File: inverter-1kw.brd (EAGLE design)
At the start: 96.6 x 100 mm, 189 parts, among them IC1 LMV358MMX, IC2 LMV358MMX, Q4 1200980569**TRANS SMD NPN MMB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, Q6 1200980569**TRANS SMD NPN MMB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, U1 ACS712, U4 ACS712, U5 SI8230, U6 SI8230, U7 ACS712, X2 https://ozdisan.com/connector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, X3 https://ozdisan.com/connector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, X7 https://ozdisan.com/connector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, X8 https://ozdisan.com/connector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

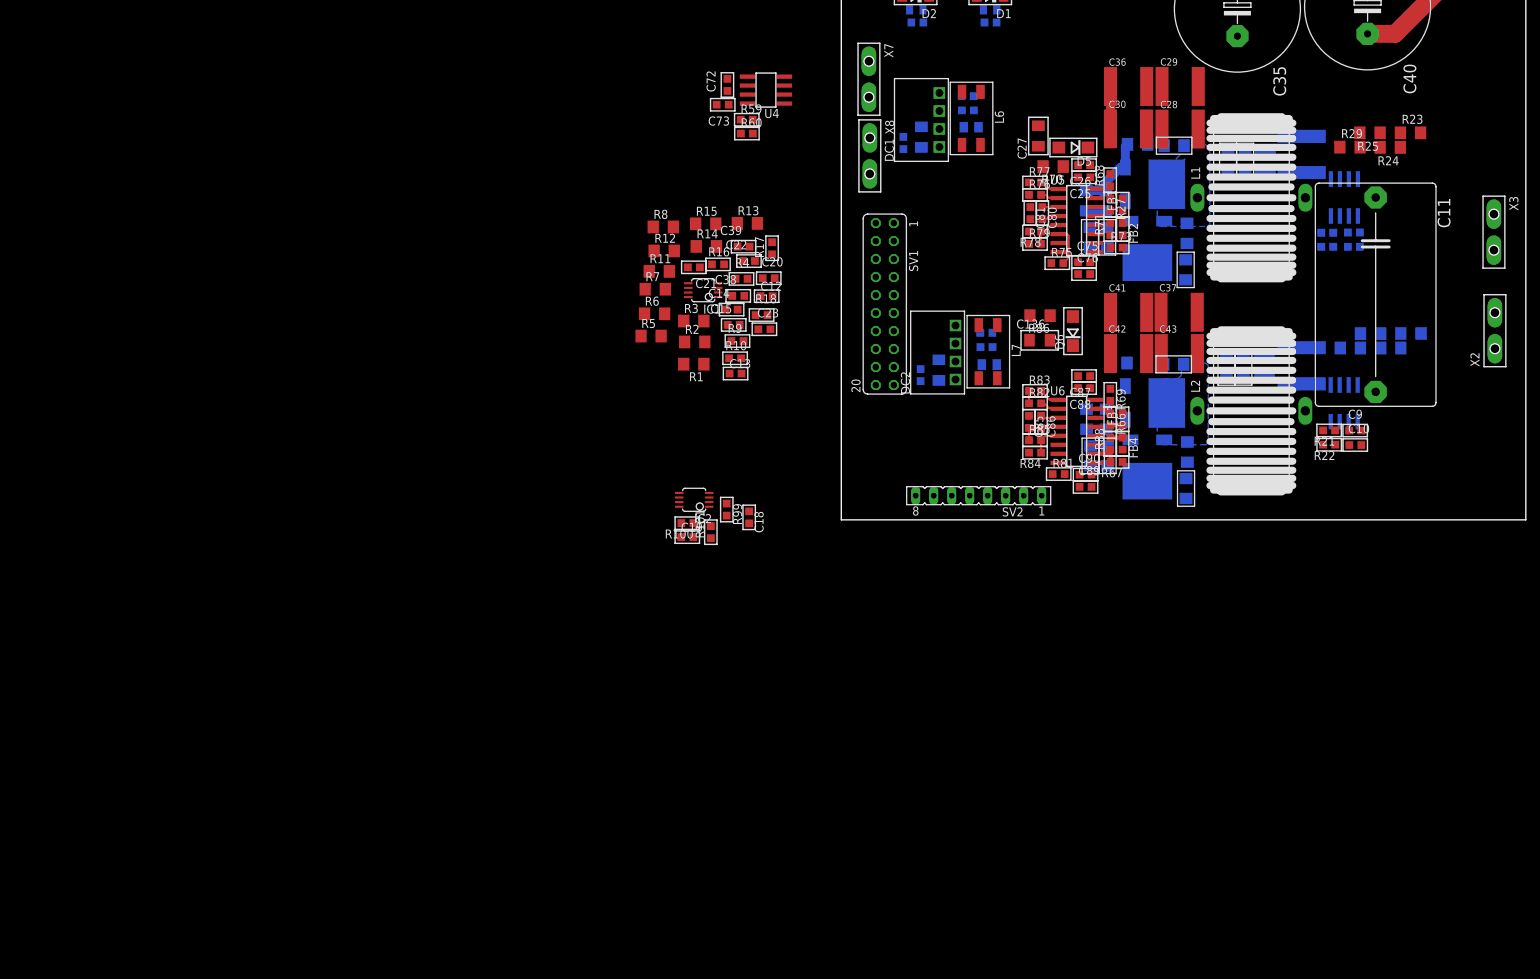
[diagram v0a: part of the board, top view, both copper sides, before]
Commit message: Giris ve cikis guc terminalleri degistirildi.
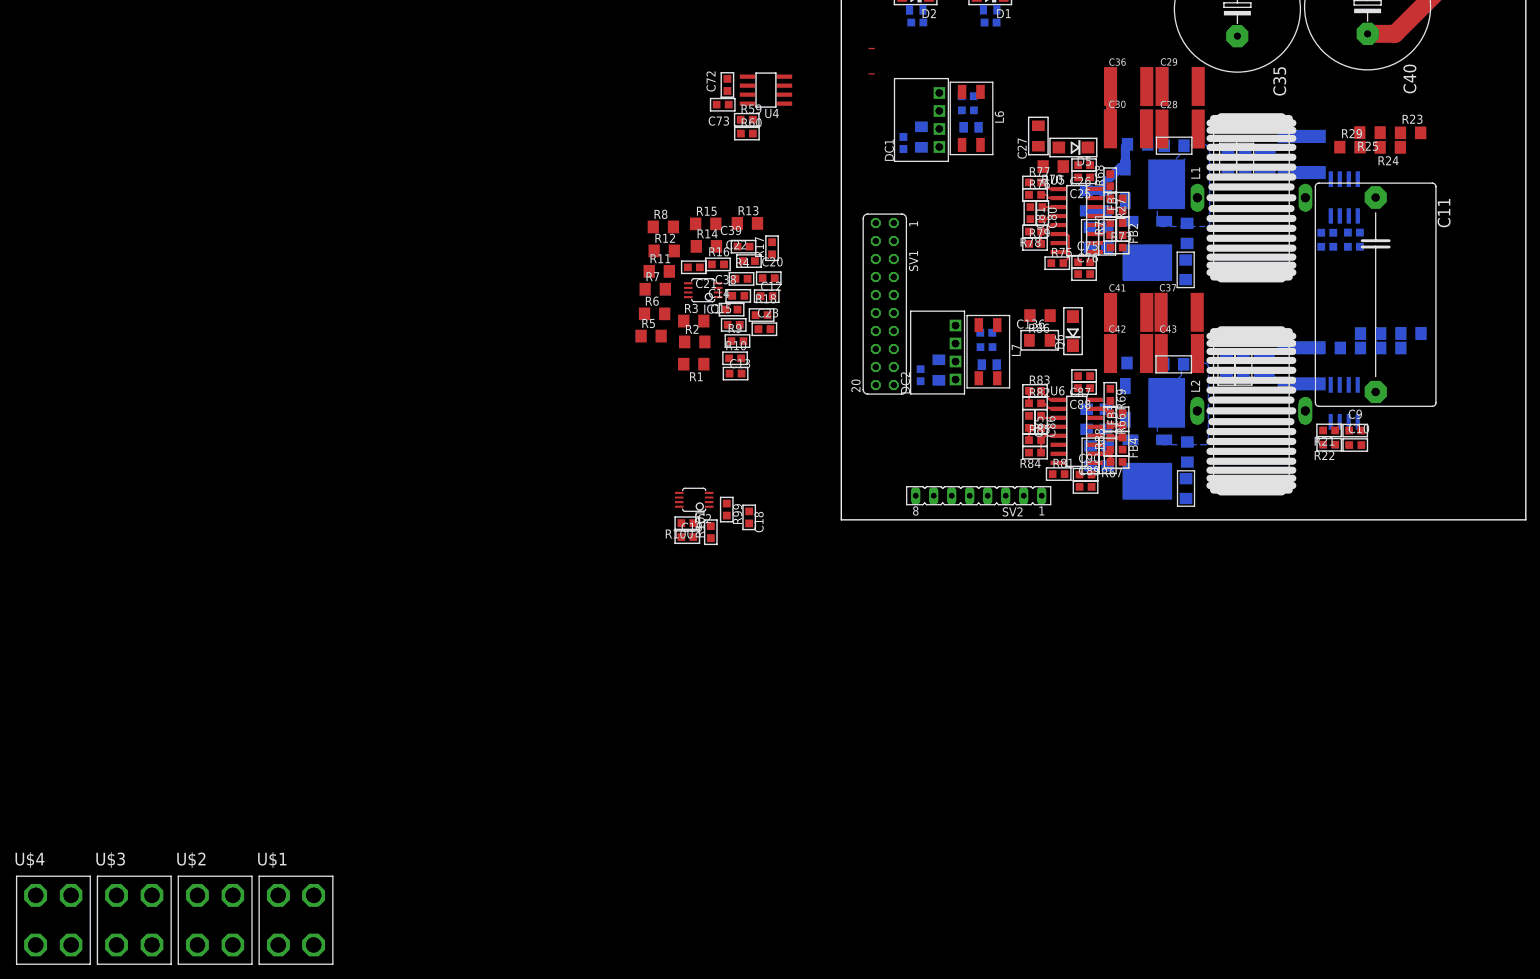
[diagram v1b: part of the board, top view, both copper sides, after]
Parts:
- removed X2, X3, X7, X8: https://ozdisan.com/connectors-and-interconnects/terminals/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, enko:RADE2
- added U$1, U$2, U$3, U$4: (no value), Andromeda:SCREWCONNECTORS(K93-01AH)
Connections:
- net AGND: now also U$2.P$1, U$2.P$2, U$2.P$3, U$2.P$4; no longer X8.1, X8.2
- net VA_OUT: now also U$4.P$1, U$4.P$2, U$4.P$3, U$4.P$4; no longer X3.1, X3.2
- net VB_OUT: now also U$3.P$1, U$3.P$2, U$3.P$3, U$3.P$4; no longer X2.1, X2.2
- net VSUPPLY+: now also U$1.P$1, U$1.P$2, U$1.P$3, U$1.P$4; no longer X7.1, X7.2

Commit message: Filtre devresi ve opamp devresi düzenlendi.
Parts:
- removed U$1, U$3, U$4: (no value), Andromeda:SCREWCONNECTORS(K93-01AH)
- added U$5, U$6, U$7: (no value), Andromeda:SCREWCONNECTORS(K93-01AH)
- moved C24 162.1 mm to (86.0, 61.6), turned to 180 degrees
- moved U$2 150.0 mm to (-9.36, 70.8), turned to 90 degrees
- moved C12 135.5 mm to (119.0, 71.5)
- moved C21 135.5 mm to (108.7, 75.5)
- moved C22 135.5 mm to (116.5, 76.4)
- moved C23 135.5 mm to (118.7, 66.8)
- moved C39 135.5 mm to (115.7, 78.5)
- moved R11 135.5 mm to (103.8, 75.0)
- moved R12 135.5 mm to (104.5, 77.8)
- moved R13 135.5 mm to (116.3, 81.7)
- moved R14 135.5 mm to (110.5, 78.5)
- moved R15 135.5 mm to (110.4, 81.7)
- moved R16 135.5 mm to (112.1, 76.0)
- moved R17 135.5 mm to (119.8, 78.2)
- moved R18 135.5 mm to (118.3, 68.8)
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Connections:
- new net N$39: C32.-, C33.-, C35.-, C37.2, C40.-, C43.2, C47.2, C48.2, C49.2, C89.2, C90.2, GN4.S, LED5.C, R28.1, R67.1, R96.1, RGND1.2, U$5.1, U$5.2, U$5.3, U$5.4, U6.9
- net AGND: no longer C32.-, C33.-, C35.-, C37.2, C40.-, C43.2, C47.2, C48.2, C49.2, C89.2, C90.2, GN4.S, LED5.C, R28.1, R67.1, R96.1, RGND1.2, U$2.P$1, U$2.P$2, U$2.P$3, U$2.P$4, U6.9
- net VA_OUT: now also U$6.1, U$6.2, U$6.3, U$6.4; no longer U$4.P$1, U$4.P$2, U$4.P$3, U$4.P$4
- net VB_OUT: now also U$7.1, U$7.2, U$7.3, U$7.4; no longer U$3.P$1, U$3.P$2, U$3.P$3, U$3.P$4
- net VSUPPLY+: now also U$2.1, U$2.2, U$2.3, U$2.4; no longer U$1.P$1, U$1.P$2, U$1.P$3, U$1.P$4
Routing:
- net N$39: track 0.00 -> 85.6 mm
- net AGND: track 67.2 -> 0.00 mm
- net DGND: track 10.1 -> 21.0 mm
- net N$7: track 0.00 -> 10.8 mm
- net N$132: track 0.00 -> 9.99 mm
- net N$9: track 0.00 -> 6.90 mm
- net N$131: track 0.00 -> 6.67 mm
- net N$18: track 0.00 -> 3.71 mm
- net GND_DRV2: track 0.00 -> 3.26 mm
- net VCC_2: track 0.00 -> 3.05 mm
- net N$16: track 0.00 -> 2.75 mm
- net N$11: track 0.00 -> 2.75 mm
- net N$10: track 0.00 -> 2.73 mm
- net +5V: track 4.80 -> 7.52 mm
- net VIN_SENS_DIFF: track 0.00 -> 2.43 mm
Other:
- board size 96.6 x 100 mm -> 97.8 x 100.1 mm

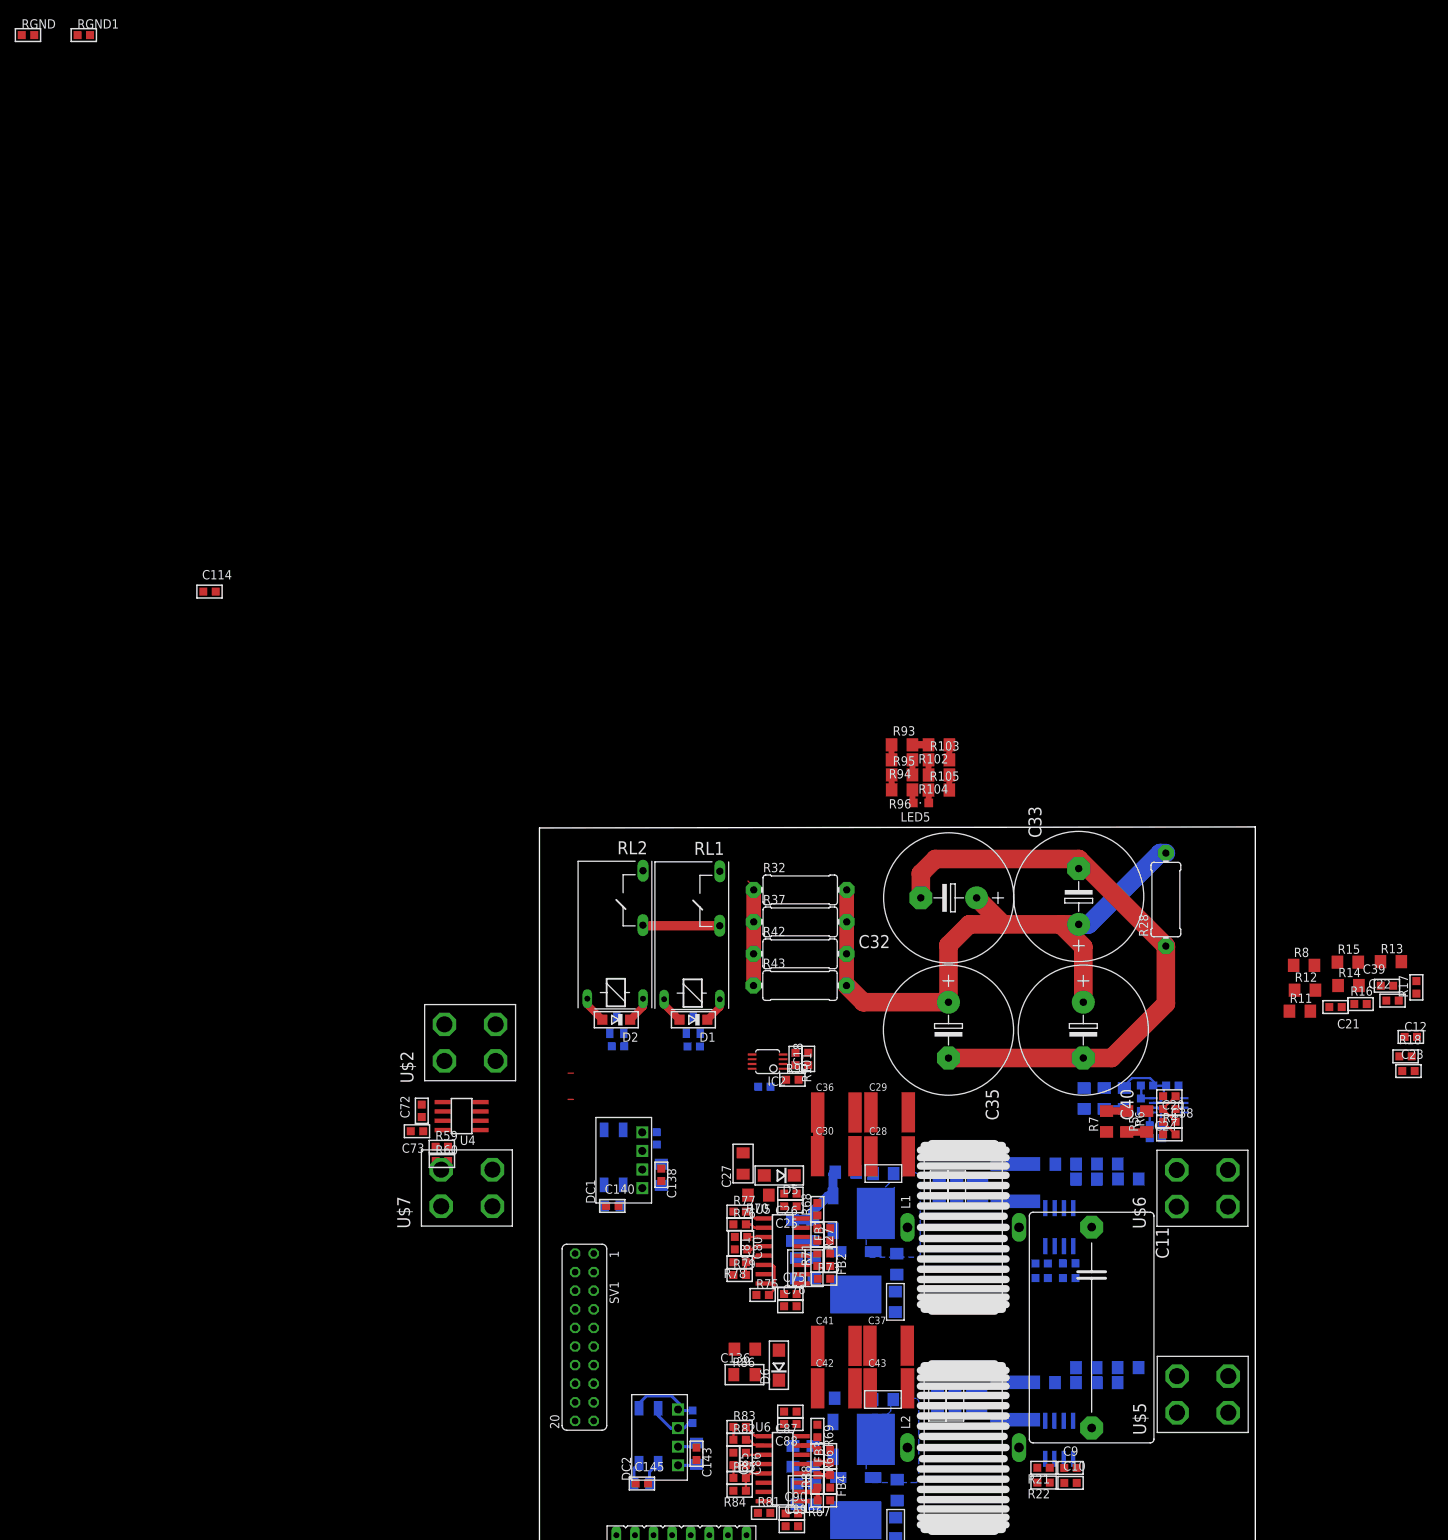
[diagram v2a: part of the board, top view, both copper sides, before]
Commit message: Opamp devresi düzenlendi
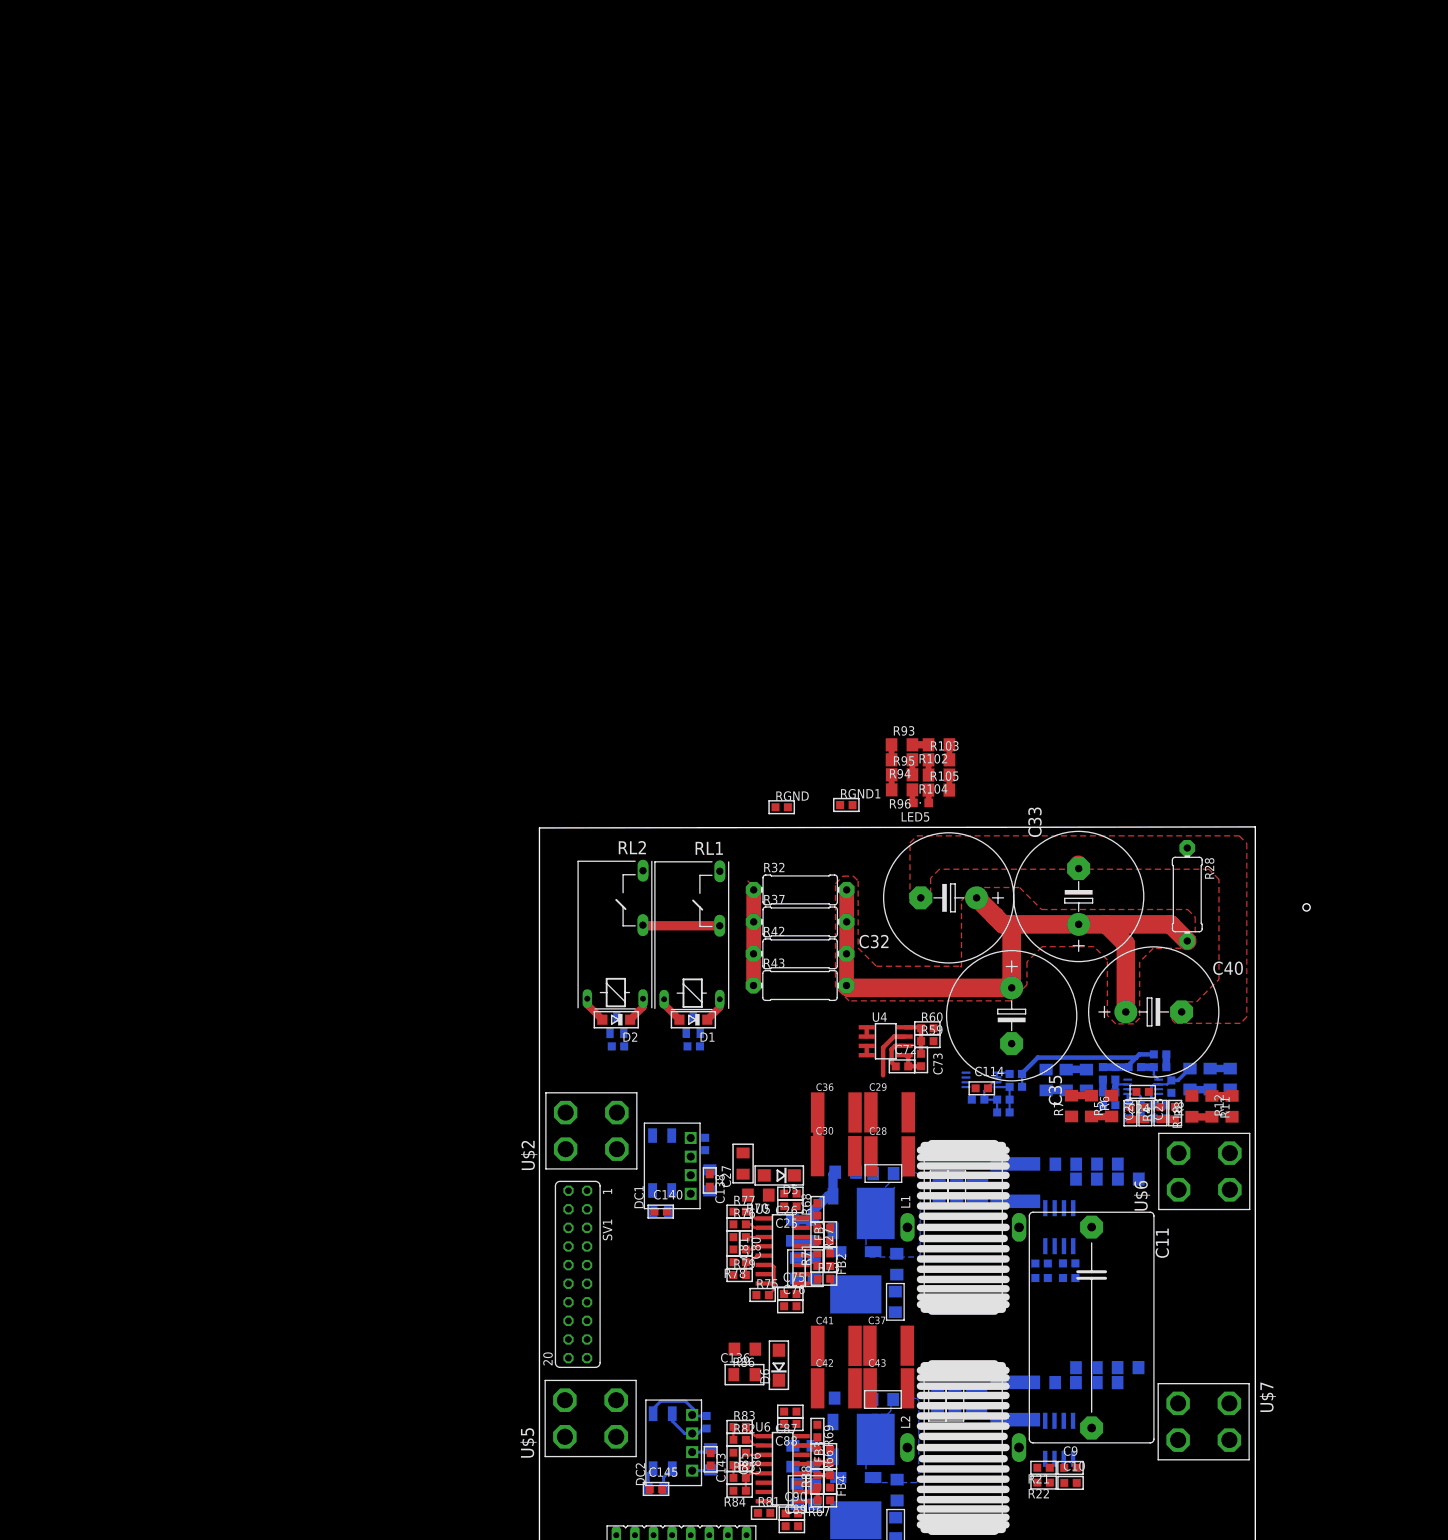
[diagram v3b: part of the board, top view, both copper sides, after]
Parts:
- moved RGND1 148.0 mm to (41.9, 103.1)
- moved RGND 147.4 mm to (33.1, 102.8)
- moved C114 125.4 mm to (60.4, 64.4)
- moved U$7 105.4 mm to (90.6, 18.8), turned to 270 degrees
- moved U$5 83.7 mm to (7.10, 19.5)
- moved C73 69.5 mm to (52.1, 68.3), turned to 270 degrees
- moved R60 68.7 mm to (53.0, 72.6)
- moved R59 67.9 mm to (53.0, 70.9)
- moved C72 65.9 mm to (49.5, 67.4), turned to 0 degrees
- moved U4 58.8 mm to (47.3, 70.9), turned to 270 degrees
- moved R17 38.6 mm to (84.7, 62.1), flipped to the bottom, turned to 180 degrees
- moved C12 36.0 mm to (84.7, 60.3), flipped to the bottom, turned to 180 degrees
- moved R18 34.4 mm to (84.8, 61.1), turned to 270 degrees
- moved C22 32.4 mm to (86.3, 64.7), flipped to the bottom, turned to 270 degrees
- moved C23 32.4 mm to (86.8, 61.1), turned to 90 degrees
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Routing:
- net N$39: track 85.6 -> 2.38 mm
- net VREF: track 0.00 -> 26.2 mm
- net N$23: track 0.00 -> 9.00 mm
- net IIN_SENS: track 0.00 -> 7.37 mm
- net N$7: track 10.8 -> 3.54 mm
- net N$1: track 0.00 -> 6.97 mm
- net N$69: track 0.00 -> 5.77 mm
- net N$70: track 0.00 -> 4.56 mm
- net DGND: track 21.0 -> 25.3 mm
- net N$20: track 0.00 -> 3.73 mm
- net N$13: track 0.00 -> 3.13 mm
- net N$17: track 0.00 -> 2.75 mm
- net N$15: track 0.00 -> 2.75 mm
- net N$12: track 0.00 -> 2.75 mm
- net N$19: track 0.00 -> 2.73 mm
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- added copper zone on layer 1, net N$39
- added copper zone on layer 1, net V_IN

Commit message: İyileştirmeler yapıldı
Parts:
- moved C139 7.67 mm to (23.7, 64.4)
- moved C140 7.67 mm to (17.6, 55.2)
- moved C141 7.67 mm to (17.6, 55.2)
- moved C138 7.67 mm to (24.3, 59.5)
- moved C142 7.67 mm to (24.3, 59.5)
- moved DC1 7.67 mm to (23.0, 61.4)
- moved L6 7.67 mm to (17.8, 61.8)
- moved C27 1.93 mm to (26.8, 52.6), turned to 180 degrees
- moved R41 0.11 mm to (10.7, 70.2)
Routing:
- net VSUPPLY+: track 10.8 -> 46.3 mm
- net V_IN: track 92.2 -> 125.6 mm
- net VDD: track 7.10 -> 23.0 mm
- net DGND: track 25.3 -> 37.8 mm, vias 0 -> 2
- net N$51: track 3.72 -> 8.80 mm
- net N$44: track 3.66 -> 8.63 mm
- net N$55: track 15.0 -> 18.8 mm
- net N$45: track 0.00 -> 1.87 mm
- net N$52: track 0.00 -> 1.76 mm
